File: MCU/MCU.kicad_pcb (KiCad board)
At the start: 2 copper layers, 107.5 x 76 mm, 72 parts, among them J1 Conn_01x02, J2 Conn_01x02, J3 Conn_01x02, J4 Conn_01x02, J5 Conn_01x02, U1 Nucleo_L432KC, U3 HHG1D-1, U4 AMC3302QDWERQ1, U5 HHG1D-1, U6 AMC3302QDWERQ1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

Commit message: Finished RTD schematic and layout. Got rid of RTD part of MCU.
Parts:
- moved FB9 37.0 mm to (137.0, 78.5)
- moved FB6 36.1 mm to (135.9, 76.0)
- moved FB3 34.7 mm to (135.9, 72.5)
- moved FB7 30.2 mm to (129.9, 118.0)
- moved FB4 22.1 mm to (135.9, 124.0)
- moved FB1 15.7 mm to (135.9, 128.5)
- moved TP1 15.0 mm to (128.5, 127.0)
- moved FB8 13.1 mm to (138.0, 94.0)
- moved RSHUNT3 9.58 mm to (127.0, 73.5)
- moved RSHUNT2 9.05 mm to (126.5, 99.0), turned to -90 degrees
- moved FB2 7.77 mm to (132.1, 102.0)
- moved R7 6.64 mm to (135.5, 97.9)
- moved FB5 5.51 mm to (131.9, 97.0)
- moved R2 5.17 mm to (139.0, 128.5), turned to 0 degrees
- moved R6 5.14 mm to (135.5, 101.9)
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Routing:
- net GND: track 44.1 -> 92.5 mm
- net +3V3: track 56.0 -> 93.6 mm, vias 3 -> 4
- net Net-(FB6-Pad1): track 0.00 -> 30.3 mm
- net Net-(U6-DCDC_HGND): track 52.4 -> 22.2 mm, vias 0 -> 2
- net Net-(FB5-Pad1): track 0.00 -> 23.1 mm
- net Net-(U4-DCDC_HGND): track 53.7 -> 30.7 mm, vias 0 -> 2
- net /LED2: track 74.7 -> 54.2 mm
- net Net-(FB4-Pad1): track 0.00 -> 16.4 mm
- net /D9: track 84.8 -> 96.2 mm
- net Net-(U6-INP): track 4.63 -> 15.7 mm
- net /LED1: track 52.8 -> 42.6 mm
- net Net-(U8-DCDC_HGND): track 21.3 -> 27.5 mm, vias 0 -> 2
- net Net-(U4-INP): track 5.52 -> 11.5 mm
- net Net-(U6-INN): track 5.36 -> 10.2 mm
- net Net-(FB6-Pad2): track 0.00 -> 3.24 mm
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
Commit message: layout suggestions
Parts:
- removed J1: Conn_01x02, Connector_Molex:Molex_CLIK-Mate_502382-0270_1x02-1MP_P1.25mm_Vertical
- removed R1: 360, Resistor_SMD:R_0805_2012Metric_Pad1.20x1.40mm_HandSolder
- removed R14: 10k, Resistor_SMD:R_0603_1608Metric_Pad0.98x0.95mm_HandSolder
- removed U9: INA333xxDGK, Package_SO:VSSOP-8_3x3mm_P0.65mm
- moved RSHUNT3 3.89 mm to (124.2, 70.8), turned to 180 degrees
- moved C16 0.44 mm to (155.7, 100.2)
- moved C17 0.20 mm to (155.7, 98.3), turned to 90 degrees
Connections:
- net Net-(J2-Pin_2) renamed +100V
- U1 pad 6: GND -> /PB0
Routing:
- net +5V: track 60.7 -> 0.00 mm
- net +100V: track 60.5 -> 0.00 mm
- net /LED3: track 49.0 -> 5.48 mm
- net Net-(FB6-Pad1): track 30.3 -> 9.37 mm
- net GND: track 92.5 -> 75.6 mm, vias 11 -> 8
- net /RTD: track 11.1 -> 0.00 mm
- net +3V3: track 93.6 -> 101.0 mm, vias 4 -> 3
- net /PA0: track 38.4 -> 35.8 mm
- net Net-(R14-Pad1): track 2.56 -> 0.00 mm
- net Net-(R14-Pad2): track 2.49 -> 0.00 mm
- added copper zone on F.Cu, net +100V
- removed copper zone on B.Cu, net +3V3

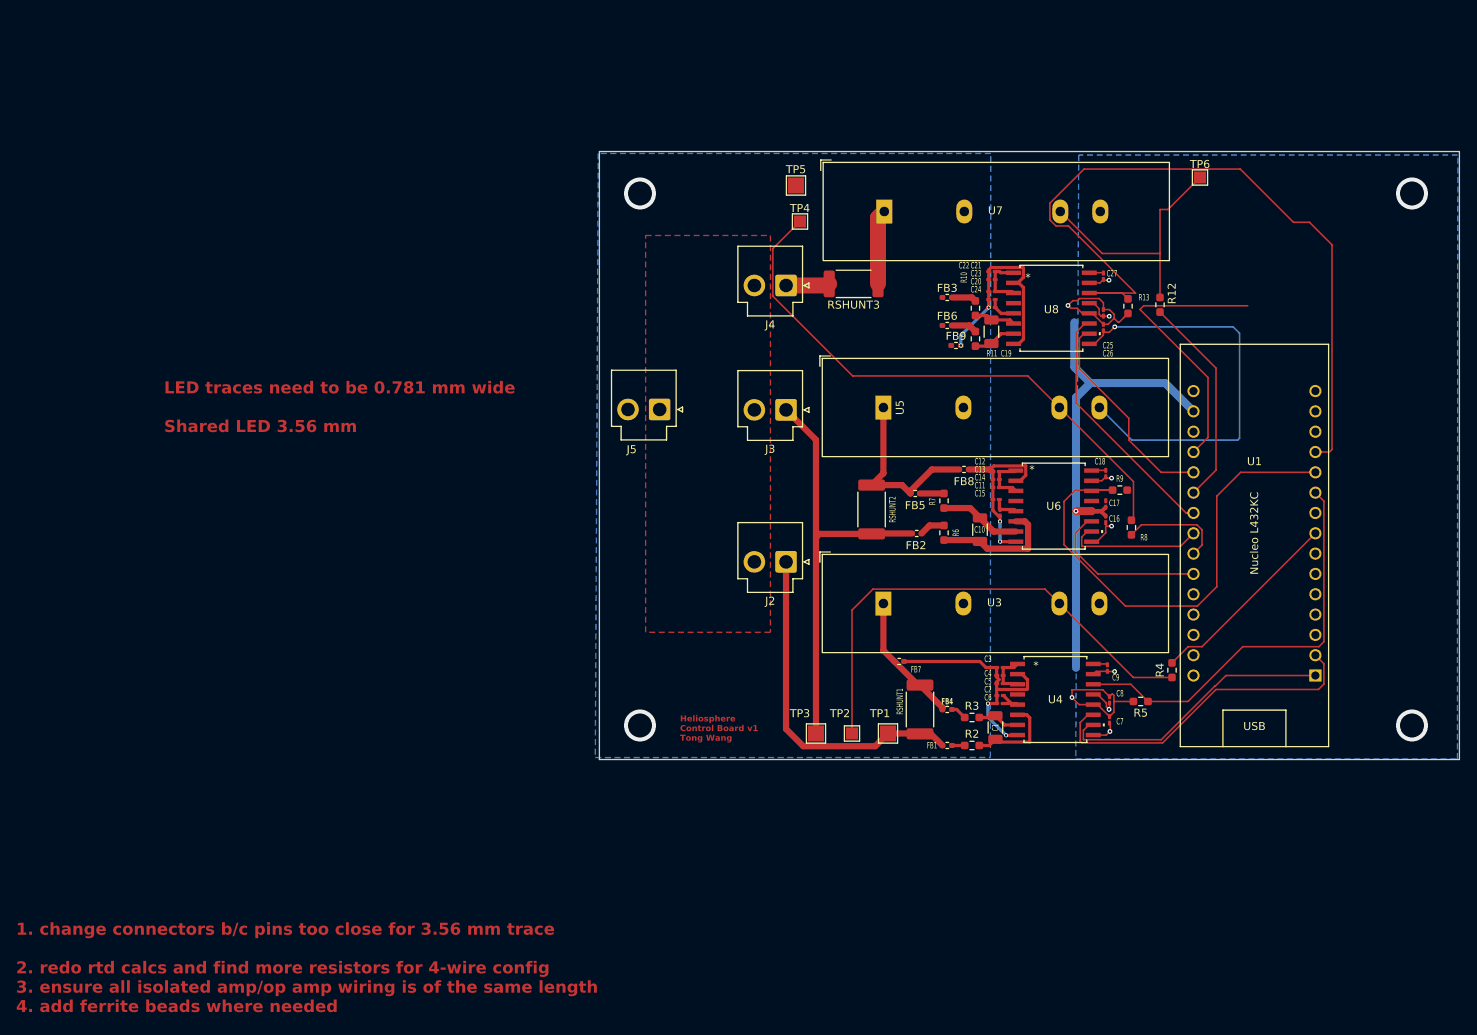
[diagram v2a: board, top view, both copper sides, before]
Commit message: Cleaned up traces in MCU layout
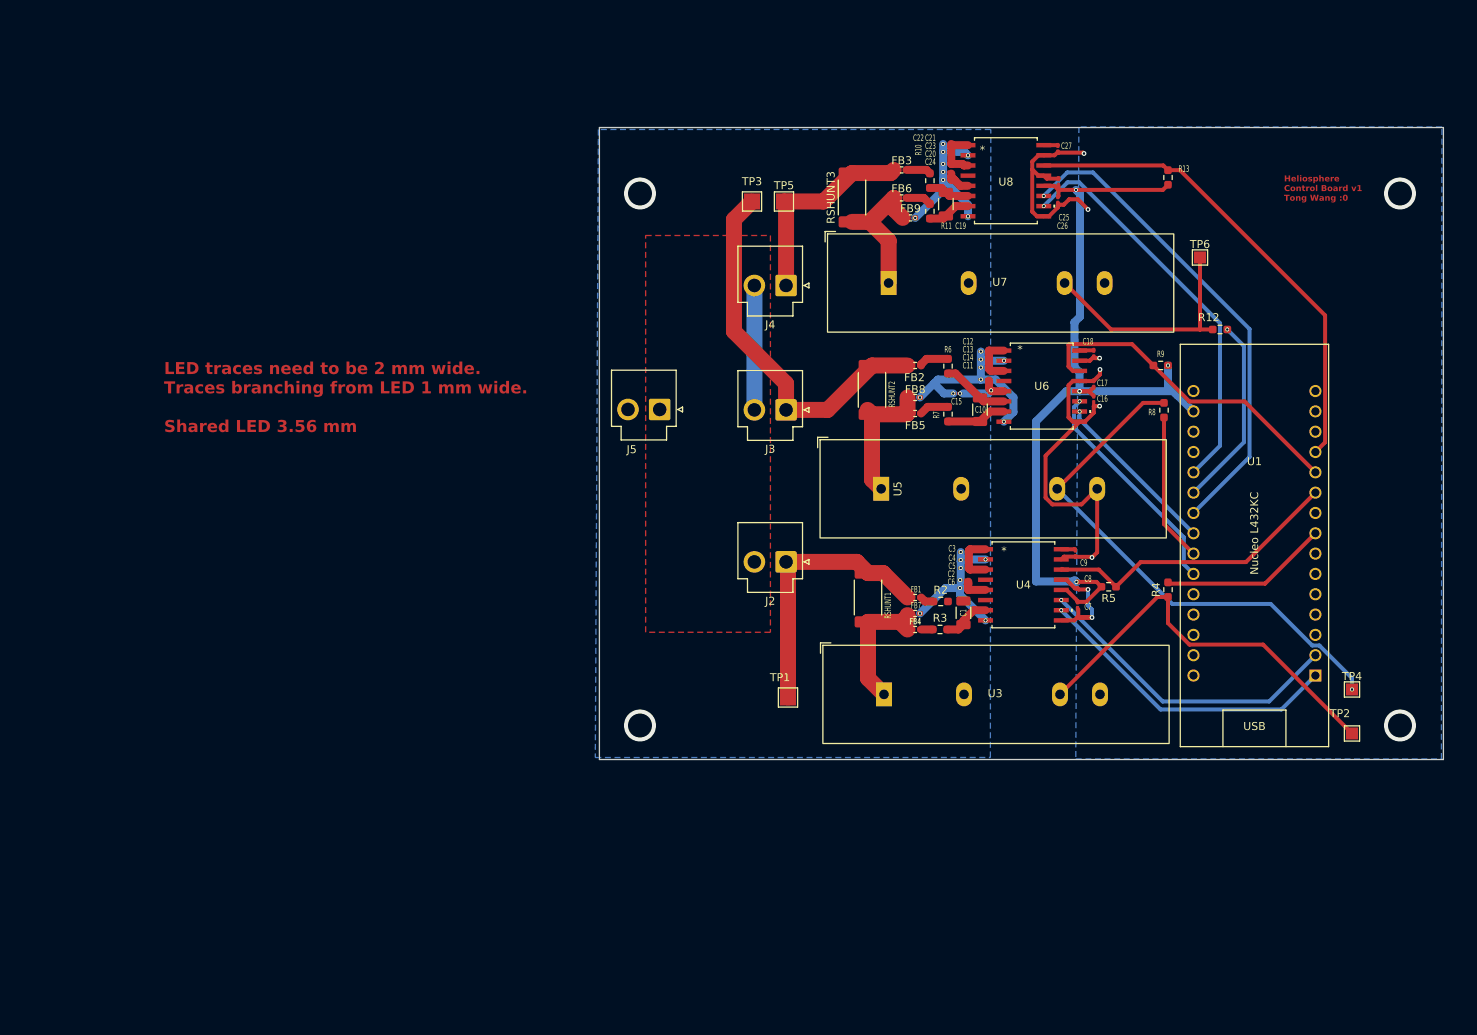
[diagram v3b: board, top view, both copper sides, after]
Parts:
- moved TP4 90.5 mm to (186.5, 121.5)
- moved TP3 67.0 mm to (111.5, 60.5)
- moved TP2 62.5 mm to (186.5, 127.0)
- moved FB2 21.0 mm to (131.9, 81.0)
- moved R6 20.8 mm to (136.0, 81.1)
- moved FB1 18.9 mm to (131.9, 110.0)
- moved R2 18.4 mm to (135.1, 110.5)
- moved C25 17.3 mm to (149.8, 58.1), turned to 90 degrees
- moved R11 16.9 mm to (133.7, 61.7)
- moved C19 16.9 mm to (135.7, 60.8)
- moved C20 16.9 mm to (135.8, 56.8)
- moved C21 16.9 mm to (135.8, 53.3)
- moved C22 16.9 mm to (135.8, 54.3)
- moved C23 16.9 mm to (135.8, 55.8)
- moved C24 16.9 mm to (135.8, 57.8)
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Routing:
- net /PA0: track 35.8 -> 0.00 mm
- net /D9: track 96.2 -> 60.5 mm
- net /PA3: track 31.3 -> 60.9 mm, vias 0 -> 1
- net /PA1: track 26.5 -> 50.6 mm, vias 0 -> 1
- net /D8: track 62.9 -> 41.9 mm
- net /LED3: track 5.48 -> 26.0 mm
- net +100V: track 0.00 -> 15.5 mm
- net /D7: track 52.0 -> 37.7 mm
- net GND: track 75.6 -> 89.5 mm
- net Net-(U4-INP): track 11.5 -> 0.00 mm
- net Net-(U4-DCDC_HGND): track 30.7 -> 19.4 mm, vias 2 -> 8
- net Net-(R4-Pad2): track 61.1 -> 50.5 mm
- net Net-(FB6-Pad1): track 9.37 -> 18.0 mm
- net /LED1: track 42.6 -> 34.1 mm
- net +3V3: track 101.0 -> 109.4 mm, vias 3 -> 4
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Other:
- board size 107.5 x 76 mm -> 105.5 x 79 mm
- board text added: "Heliosphere Control Board v1 Tong Wang :0"
- board text added: "LED traces need to be 2 mm wide. Traces branching from LED 1 mm wide. Shared LED 3.56 mm"
- board text removed: "1. change connectors b/c pins too close for 3.56 mm trace 2. redo rtd calcs and find more resistors for 4-wire config 3. ensure all isolated amp/op amp wiring is of the same length 4. add ferrite beads where needed"
- board text removed: "Heliosphere Control Board v1 Tong Wang"
- board text removed: "LED traces need to be 0.781 mm wide Shared LED 3.56 mm"

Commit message: layout changes
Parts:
- moved TP4 34.0 mm to (157.0, 104.6)
- moved TP2 27.9 mm to (161.8, 114.0)
- moved R8 17.1 mm to (161.8, 103.6), turned to 180 degrees
- moved U1 13.3 mm to (182.6, 91.5)
- moved FB9 8.97 mm to (128.6, 54.0)
- moved R9 5.45 mm to (157.6, 83.2), turned to -90 degrees
- moved FB6 4.21 mm to (127.2, 63.0)
- moved R11 3.76 mm to (130.2, 63.0), turned to 0 degrees
- moved R10 3.65 mm to (130.2, 57.0), turned to 0 degrees
- moved FB3 3.05 mm to (127.2, 57.0)
- moved C19 2.67 mm to (133.2, 60.0)
- moved C26 0.68 mm to (149.8, 59.6)
- moved C16 0.58 mm to (154.8, 85.2)
- moved C17 0.58 mm to (154.8, 83.3)
- moved C25 0.40 mm to (149.8, 57.7)
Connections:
- R12 pad 1: /PA2 -> /LED CONTROLS 3/CTRL
- R8 pad 1: /PA5 -> /LED CONTROLS 2/CTRL
- U6 pad 10: /PA4 -> /PA3
- U6 pad 11: /PA6 -> /PA2
- U8 pad 10: /PA1 -> /PA0
- U8 pad 11: /PA3 -> /PA1
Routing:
- net GND: track 89.5 -> 23.0 mm, vias 8 -> 6
- net Net-(R8-Pad2): track 65.9 -> 0.00 mm, vias 1 -> 0
- net /D9: track 60.5 -> 15.8 mm
- net /PA0: track 0.00 -> 41.6 mm
- net +3V3: track 109.4 -> 68.7 mm, vias 4 -> 2
- net /PA10: track 39.4 -> 0.00 mm, vias 1 -> 0
- net /PA9: track 38.7 -> 0.00 mm, vias 1 -> 0
- net /PA3: track 60.9 -> 23.4 mm, vias 1 -> 0
- net /D8: track 41.9 -> 5.40 mm
- net Net-(R4-Pad2): track 50.5 -> 18.5 mm
- net /D7: track 37.7 -> 7.86 mm
- net /PA6: track 28.0 -> 0.00 mm, vias 1 -> 0
- net /PA4: track 21.1 -> 0.00 mm, vias 1 -> 0
- net /PB6: track 21.1 -> 0.00 mm
- net /PA5: track 18.5 -> 0.00 mm
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
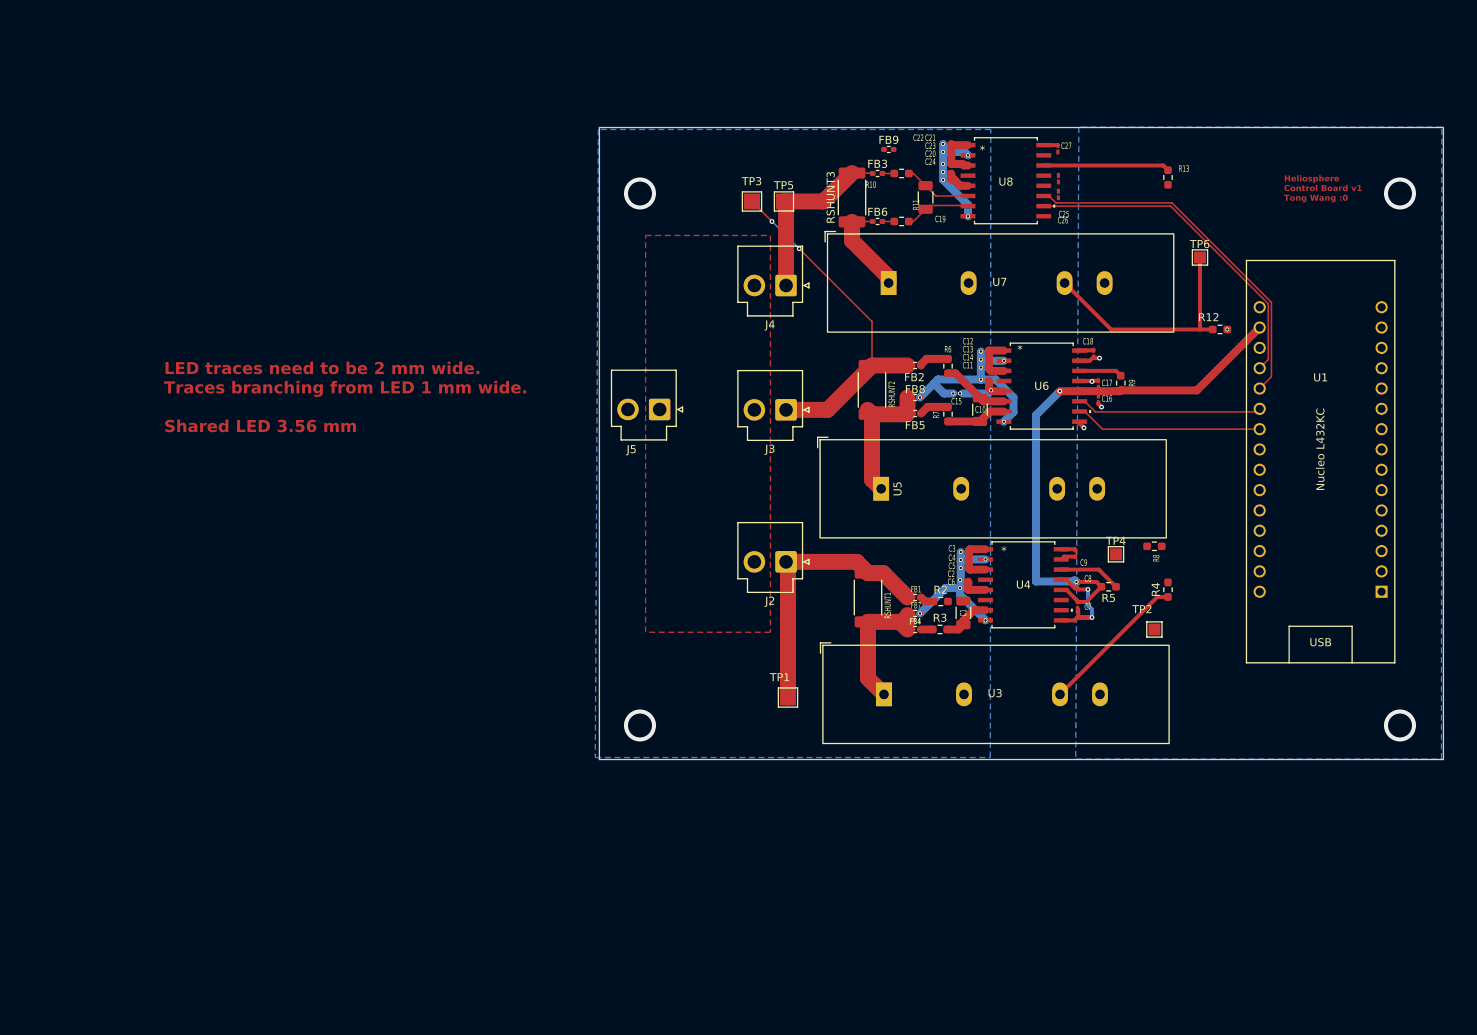
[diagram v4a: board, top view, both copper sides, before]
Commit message: almost done with MCU: need to change TP names, adjust RTD on MCU
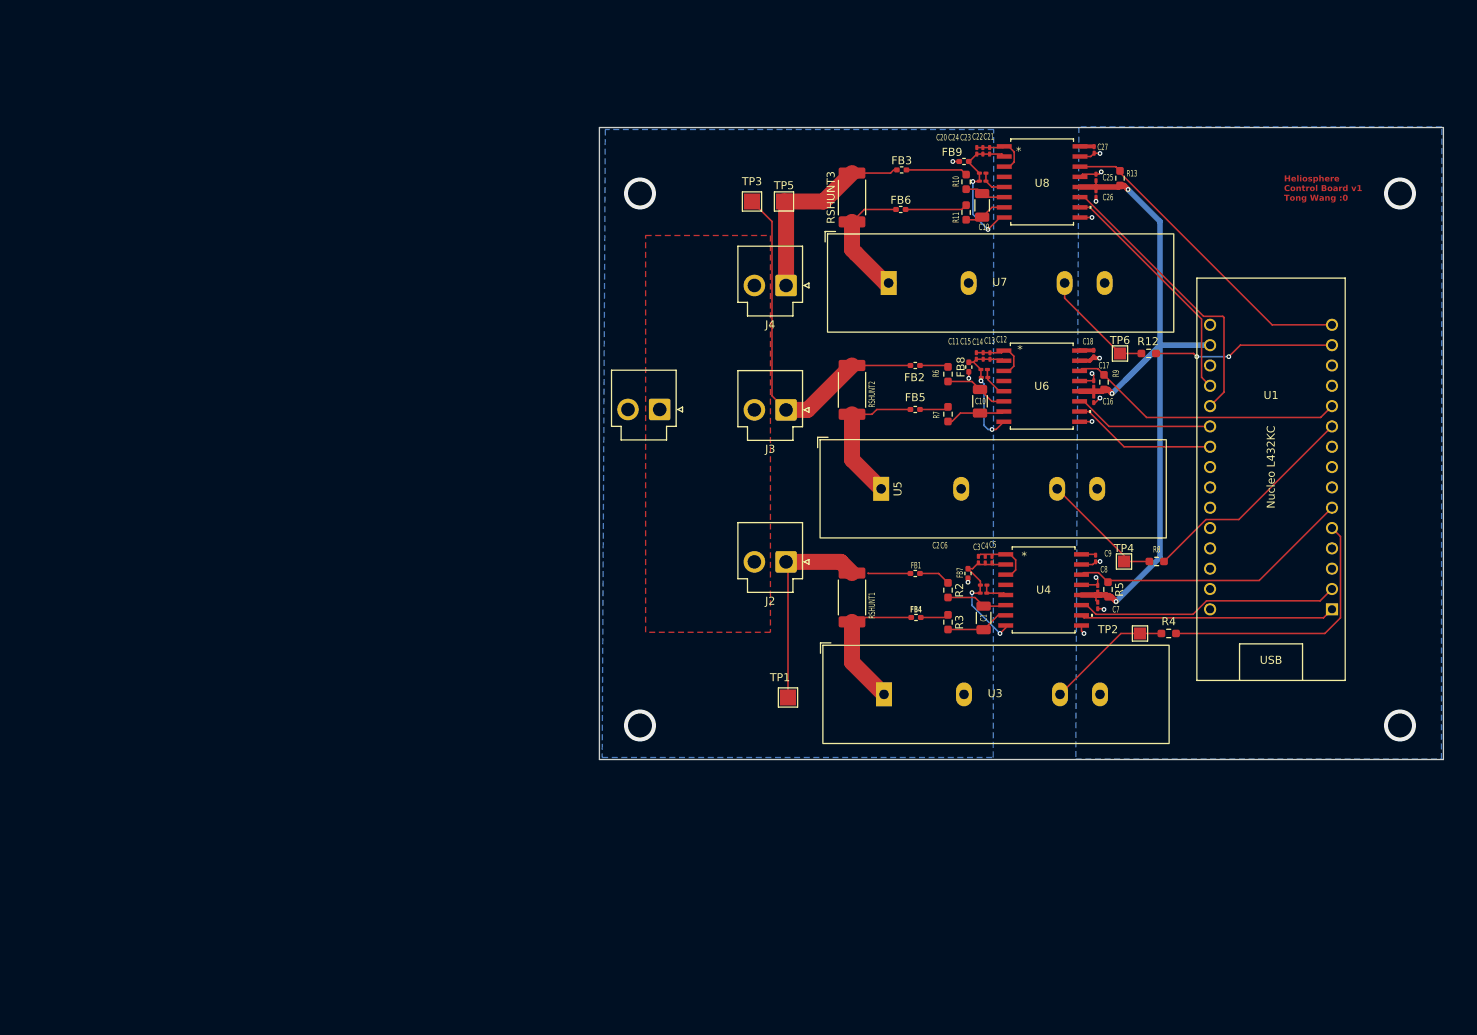
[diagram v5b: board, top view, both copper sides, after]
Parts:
- moved TP6 15.6 mm to (157.5, 79.5)
- moved FB9 9.52 mm to (138.0, 55.5)
- moved R12 9.40 mm to (161.1, 79.5)
- moved FB7 8.28 mm to (138.5, 107.0), turned to 90 degrees
- moved R11 8.14 mm to (138.3, 61.9), turned to -90 degrees
- moved R10 8.13 mm to (138.3, 58.0), turned to -90 degrees
- moved FB8 7.70 mm to (138.6, 81.2), turned to 90 degrees
- moved C19 7.13 mm to (140.3, 61.0)
- moved U1 6.58 mm to (176.4, 93.7)
- moved R13 6.00 mm to (157.5, 57.6)
- moved C23 5.64 mm to (141.2, 54.2), turned to -90 degrees
- moved R4 5.48 mm to (163.6, 114.5), turned to 180 degrees
- moved C26 4.70 mm to (154.5, 59.6)
- moved C25 4.69 mm to (154.5, 57.5)
- moved C22 4.56 mm to (140.4, 54.2), turned to -90 degrees
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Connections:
- FB7 pad 1: Net-(FB4-Pad1) -> GND1
- FB8 pad 1: Net-(FB5-Pad1) -> GND1
- FB9 pad 1: Net-(FB6-Pad1) -> GND1
- R12 pad 1: /LED CONTROLS 3/CTRL -> /D11
- R13 pad 1: /D9 -> /D12
- R4 pad 1: /PB6 -> /D2
- R5 pad 1: /D7 -> /PB0
- R8 pad 1: /LED CONTROLS 2/CTRL -> /D7
- U1 pad 12: /D9 -> unconnected-(U1-D9-Pad12)
- U1 pad 14: unconnected-(U1-D11-Pad14) -> /D11
- U1 pad 15: unconnected-(U1-D12-Pad15) -> /D12
- U1 pad 5: unconnected-(U1-D2-Pad5) -> /D2
- U4 pad 14: /D7 -> /PB0
- U8 pad 14: /D9 -> /D12
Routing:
- net /D12: track 0.00 -> 39.8 mm
- net /PB0: track 0.00 -> 35.8 mm
- net /PA10: track 0.00 -> 33.1 mm
- net /D2: track 0.00 -> 33.0 mm
- net /PA9: track 0.00 -> 31.9 mm
- net /D8: track 5.40 -> 34.8 mm
- net +3V3: track 68.7 -> 93.7 mm, vias 2 -> 3
- net /D11: track 0.00 -> 22.8 mm, vias 0 -> 2
- net /D7: track 7.86 -> 28.0 mm
- net /D9: track 15.8 -> 0.00 mm
- net Net-(R8-Pad2): track 0.00 -> 15.7 mm
- net Net-(R12-Pad2): track 29.9 -> 14.3 mm
- net /PA0: track 41.6 -> 29.8 mm
- net Net-(U6-DCDC_HGND): track 27.1 -> 16.9 mm, vias 8 -> 2
- net /PA1: track 45.3 -> 36.0 mm
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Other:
- board text removed: "LED traces need to be 2 mm wide. Traces branching from LED 1 mm wide. Shared LED 3.56 mm"
